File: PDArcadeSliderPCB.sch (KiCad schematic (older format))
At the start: 8 parts, among them J1 Conn_01x06_Male, J2 Conn_01x06_Male, U1 testsensorg, U2 testsensorg, U3 testsensorg, U4 testsensorg, U5 testsensorg, U6 testsensorg

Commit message: some changes for beauty
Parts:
- removed U1, U2, U3, U4, U5, U6: testsensorg, testlibrary:sensorg, symbol testsensorlib:testsensorg
- added U1, U2, U3, U4, U5, U6: testsensorg, symbol test:testsensorg
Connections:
- wire segments 23 -> 21
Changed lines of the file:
@@
 EESchema Schematic File Version 4
-EELAYER 26 0
+EELAYER 30 0
 EELAYER END
 $Descr A4 11693 8268
@@
 	1    0    0    -1
 $EndComp
-$Comp
-L testsensorlib:testsensorg U1
-U 1 1 5C3C1C0C
-P 8100 2600
-F 0 "U1" H 8678 2046 50  0000 L CNN
-F 1 "testsensorg" H 8678 1955 50  0000 L CNN
-F 2 "testlibrary:sensorg" H 8100 2600 50  0001 C CNN
-F 3 "" H 8100 2600 50  0001 C CNN
-	1    8100 2600
-	1    0    0    -1
-$EndComp
-Wire Wire Line
-	8200 3200 7800 3200
 Wire Wire Line
 	7800 3200 7800 3400
 Wire Wire Line
 	7800 3400 7500 3400
-$Comp
-L testsensorlib:testsensorg U4
-U 1 1 5C3C1D40
-P 8500 2800
-F 0 "U4" H 9078 2246 50  0000 L CNN
-F 1 "testsensorg" H 9078 2155 50  0000 L CNN
-F 2 "testlibrary:sensorg" H 8500 2800 50  0001 C CNN
-F 3 "" H 8500 2800 50  0001 C CNN
-	1    8500 2800
-	1    0    0    -1
-$EndComp
-$Comp
-L testsensorlib:testsensorg U2
-U 1 1 5C3C1DA6
-P 8100 3000
-F 0 "U2" H 8678 2446 50  0000 L CNN
-F 1 "testsensorg" H 8678 2355 50  0000 L CNN
-F 2 "testlibrary:sensorg" H 8100 3000 50  0001 C CNN
-F 3 "" H 8100 3000 50  0001 C CNN
-	1    8100 3000
-	1    0    0    -1
-$EndComp
-$Comp
-L testsensorlib:testsensorg U5
-U 1 1 5C3C1E08
-P 8500 3200
-F 0 "U5" H 9078 2646 50  0000 L CNN
-F 1 "testsensorg" H 9078 2555 50  0000 L CNN
-F 2 "testlibrary:sensorg" H 8500 3200 50  0001 C CNN
-F 3 "" H 8500 3200 50  0001 C CNN
-	1    8500 3200
-	1    0    0    -1
-$EndComp
-$Comp
-L testsensorlib:testsensorg U3
-U 1 1 5C3C1E58
-P 8100 3400
-F 0 "U3" H 8678 2846 50  0000 L CNN
-F 1 "testsensorg" H 8678 2755 50  0000 L CNN
-F 2 "testlibrary:sensorg" H 8100 3400 50  0001 C CNN
-F 3 "" H 8100 3400 50  0001 C CNN
-	1    8100 3400
-	1    0    0    -1
-$EndComp
-$Comp
-L testsensorlib:testsensorg U6
-U 1 1 5C3C1E94
-P 8500 3600
-F 0 "U6" H 9078 3046 50  0000 L CNN
-F 1 "testsensorg" H 9078 2955 50  0000 L CNN
-F 2 "testlibrary:sensorg" H 8500 3600 50  0001 C CNN
-F 3 "" H 8500 3600 50  0001 C CNN
-	1    8500 3600
-	1    0    0    -1
-$EndComp
-Wire Wire Line
-	8600 3400 7850 3400
 Wire Wire Line
 	7850 3400 7850 3500
 Wire Wire Line
 	7850 3500 7500 3500
-Wire Wire Line
-	7500 3600 8200 3600
-Wire Wire Line
-	8250 3700 8250 3800
-Wire Wire Line
-	8250 3800 8600 3800
-Wire Wire Line
-	7500 3700 8250 3700
-Wire Wire Line
-	8200 4000 8200 3800
-Wire Wire Line
-	8200 3800 7500 3800
-Wire Wire Line
-	8600 4200 8100 4200
-Wire Wire Line
-	8100 4200 8100 3900
-Wire Wire Line
-	8100 3900 7500 3900
 $Comp
 L Connector:Conn_01x06_Male J2
@@
 $EndComp
 Wire Wire Line
-	9250 2850 9250 1450
-Wire Wire Line
-	9250 1450 10350 1450
-Wire Wire Line
 	7500 3400 6950 3400
 Connection ~ 7500 3400
@@
 Wire Wire Line
 	6950 3700 7500 3700
+Wire Wire Line
+	7500 3800 6950 3800
+Wire Wire Line
+	6950 3900 7500 3900
+$Comp
+L test:testsensorg U1
+U 1 1 5DDFA193
+P 8000 2600
+F 0 "U1" H 8578 2046 50  0000 L CNN
+F 1 "testsensorg" H 8578 1955 50  0000 L CNN
+F 2 "" H 8000 2600 50  0001 C CNN
+F 3 "" H 8000 2600 50  0001 C CNN
+	1    8000 2600
+	1    0    0    -1
+$EndComp
+$Comp
+L test:testsensorg U2
+U 1 1 5DDFB269
+P 8000 2800
+F 0 "U2" H 8578 2246 50  0000 L CNN
+F 1 "testsensorg" H 8578 2155 50  0000 L CNN
+F 2 "" H 8000 2800 50  0001 C CNN
+F 3 "" H 8000 2800 50  0001 C CNN
+	1    8000 2800
+	1    0    0    -1
+$EndComp
+$Comp
+L test:testsensorg U3
+U 1 1 5DDFE35C
+P 8000 3000
+F 0 "U3" H 8578 2446 50  0000 L CNN
+F 1 "testsensorg" H 8578 2355 50  0000 L CNN
+F 2 "" H 8000 3000 50  0001 C CNN
+F 3 "" H 8000 3000 50  0001 C CNN
+	1    8000 3000
+	1    0    0    -1
+$EndComp
+Wire Wire Line
+	7500 3600 8100 3600
+$Comp
+L test:testsensorg U4
+U 1 1 5DE011FA
+P 8000 3200
+F 0 "U4" H 8578 2646 50  0000 L CNN
+F 1 "testsensorg" H 8578 2555 50  0000 L CNN
+F 2 "" H 8000 3200 50  0001 C CNN
+F 3 "" H 8000 3200 50  0001 C CNN
+	1    8000 3200
+	1    0    0    -1
+$EndComp
+$Comp
+L test:testsensorg U5
+U 1 1 5DE01935
+P 8000 3400
+F 0 "U5" H 8578 2846 50  0000 L CNN
+F 1 "testsensorg" H 8578 2755 50  0000 L CNN
+F 2 "" H 8000 3400 50  0001 C CNN
+F 3 "" H 8000 3400 50  0001 C CNN
+	1    8000 3400
+	1    0    0    -1
+$EndComp
+$Comp
+L test:testsensorg U6
+U 1 1 5DE01F95
+P 8000 3600
+F 0 "U6" H 8578 3046 50  0000 L CNN
+F 1 "testsensorg" H 8578 2955 50  0000 L CNN
+F 2 "" H 8000 3600 50  0001 C CNN
+F 3 "" H 8000 3600 50  0001 C CNN
+	1    8000 3600
+	1    0    0    -1
+$EndComp
+Wire Wire Line
+	7850 3400 8100 3400
+Wire Wire Line
+	7800 3200 8100 3200
+Wire Wire Line
+	7500 3700 8100 3700
+Wire Wire Line
+	8100 3700 8100 3800
 Connection ~ 7500 3700
 Wire Wire Line
-	7500 3800 6950 3800
+	7500 3800 8050 3800
+Wire Wire Line
+	8050 3800 8050 4000
+Wire Wire Line
+	8050 4000 8100 4000
 Connection ~ 7500 3800
 Wire Wire Line
-	6950 3900 7500 3900
+	7500 3900 8000 3900
+Wire Wire Line
+	8000 3900 8000 4200
+Wire Wire Line
+	8000 4200 8100 4200
 Connection ~ 7500 3900
 $EndSCHEMATC

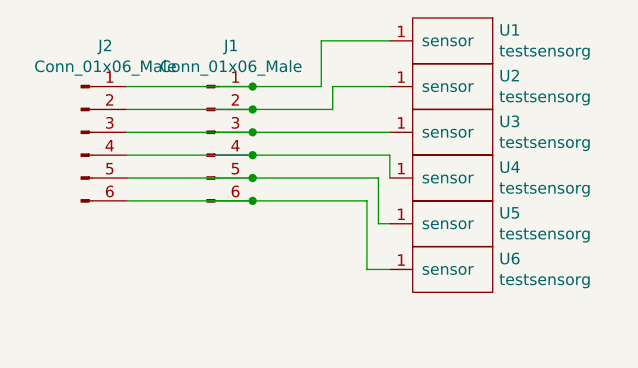
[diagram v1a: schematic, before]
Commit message: Added ground hatching to PCB
Added ground hatching to PCB to decrease parasitic capacitance
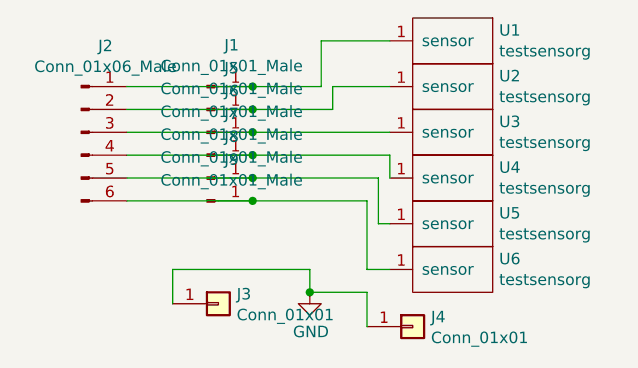
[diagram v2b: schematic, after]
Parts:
- removed J1: Conn_01x06_Male, Connector_PinHeader_1.27mm:PinHeader_1x06_P1.27mm_Vertical, symbol Connector:Conn_01x06_Male
- added J1, J5, J6, J7, J8, J9: Conn_01x01_Male, Connector_PinHeader_1.27mm:PinHeader_1x01_P1.27mm_Vertical, symbol Connector:Conn_01x01_Male
- added J3, J4: Conn_01x01, Connector_PinSocket_2.54mm:PinSocket_1x01_P2.54mm_Horizontal, symbol Connector_Generic:Conn_01x01
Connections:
- net at J2.1 (Pin_1), U1.1 (sensor): now also J1.1 (Pin_1)
- net at J2.2 (Pin_2), U2.1 (sensor): now also J5.1 (Pin_1)
- net at J2.3 (Pin_3), U3.1 (sensor): now also J6.1 (Pin_1)
- net at J2.4 (Pin_4), U4.1 (sensor): now also J7.1 (Pin_1)
- net at J2.5 (Pin_5), U5.1 (sensor): now also J8.1 (Pin_1)
- net at J2.6 (Pin_6), U6.1 (sensor): now also J9.1 (Pin_1)
- new net GND: J3.1 (Pin_1), J4.1 (Pin_1)
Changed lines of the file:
@@
-EESchema Schematic File Version 4
+EESchema Schematic File Version 5
 EELAYER 30 0
 EELAYER END
@@
 Comment3 ""
 Comment4 ""
+Comment5 ""
+Comment6 ""
+Comment7 ""
+Comment8 ""
+Comment9 ""
 $EndDescr
-$Comp
-L Connector:Conn_01x06_Male J1
-U 1 1 5C3BAF9E
-P 7300 3600
-F 0 "J1" H 7406 3978 50  0000 C CNN
-F 1 "Conn_01x06_Male" H 7406 3887 50  0000 C CNN
-F 2 "Connector_PinHeader_1.27mm:PinHeader_1x06_P1.27mm_Vertical" H 7300 3600 50  0001 C CNN
-F 3 "~" H 7300 3600 50  0001 C CNN
-	1    7300 3600
-	1    0    0    -1
-$EndComp
 Wire Wire Line
 	7800 3200 7800 3400
 Wire Wire Line
-	7800 3400 7500 3400
-Wire Wire Line
 	7850 3400 7850 3500
-Wire Wire Line
-	7850 3500 7500 3500
 $Comp
 L Connector:Conn_01x06_Male J2
@@
 	1    0    0    -1
 $EndComp
-Wire Wire Line
-	7500 3400 6950 3400
-Connection ~ 7500 3400
-Wire Wire Line
-	6950 3500 7500 3500
-Connection ~ 7500 3500
-Wire Wire Line
-	7500 3600 6950 3600
-Connection ~ 7500 3600
-Wire Wire Line
-	6950 3700 7500 3700
-Wire Wire Line
-	7500 3800 6950 3800
-Wire Wire Line
-	6950 3900 7500 3900
 $Comp
 L test:testsensorg U1
@@
 	1    0    0    -1
 $EndComp
-Wire Wire Line
-	7500 3600 8100 3600
 $Comp
 L test:testsensorg U4
@@
 	7800 3200 8100 3200
 Wire Wire Line
+	8100 3700 8100 3800
+Wire Wire Line
+	8050 3800 8050 4000
+Wire Wire Line
+	8050 4000 8100 4000
+Wire Wire Line
+	8000 3900 8000 4200
+Wire Wire Line
+	8000 4200 8100 4200
+$Comp
+L power:GND #PWR0101
+U 1 1 5DEF6165
+P 7750 4300
+F 0 "#PWR0101" H 7750 4050 50  0001 C CNN
+F 1 "GND" H 7755 4127 50  0000 C CNN
+F 2 "" H 7750 4300 50  0001 C CNN
+F 3 "" H 7750 4300 50  0001 C CNN
+	1    7750 4300
+	1    0    0    -1
+$EndComp
+$Comp
+L Connector_Generic:Conn_01x01 J3
+U 1 1 5DEF9922
+P 7350 4350
+F 0 "J3" H 7430 4392 50  0000 L CNN
+F 1 "Conn_01x01" H 7430 4301 50  0000 L CNN
+F 2 "Connector_PinSocket_2.54mm:PinSocket_1x01_P2.54mm_Horizontal" H 7350 4350 50  0001 C CNN
+F 3 "~" H 7350 4350 50  0001 C CNN
+	1    7350 4350
+	1    0    0    -1
+$EndComp
+$Comp
+L Connector_Generic:Conn_01x01 J4
+U 1 1 5DEFB162
+P 8200 4450
+F 0 "J4" H 8280 4492 50  0000 L CNN
+F 1 "Conn_01x01" H 8280 4401 50  0000 L CNN
+F 2 "Connector_PinSocket_2.54mm:PinSocket_1x01_P2.54mm_Horizontal" H 8200 4450 50  0001 C CNN
+F 3 "~" H 8200 4450 50  0001 C CNN
+	1    8200 4450
+	1    0    0    -1
+$EndComp
+Wire Wire Line
+	8000 4450 8000 4300
+Wire Wire Line
+	8000 4300 7750 4300
+Connection ~ 7750 4300
+Wire Wire Line
+	7150 4350 7150 4200
+Wire Wire Line
+	7150 4200 7750 4200
+Wire Wire Line
+	7750 4200 7750 4300
+Wire Wire Line
+	6950 3400 7500 3400
+Wire Wire Line
+	7500 3400 7800 3400
+Connection ~ 7500 3400
+$Comp
+L Connector:Conn_01x01_Male J1
+U 1 1 5DEF97FC
+P 7300 3400
+F 0 "J1" H 7408 3581 50  0000 C CNN
+F 1 "Conn_01x01_Male" H 7408 3490 50  0000 C CNN
+F 2 "Connector_PinHeader_1.27mm:PinHeader_1x01_P1.27mm_Vertical" H 7300 3400 50  0001 C CNN
+F 3 "~" H 7300 3400 50  0001 C CNN
+	1    7300 3400
+	1    0    0    -1
+$EndComp
+$Comp
+L Connector:Conn_01x01_Male J5
+U 1 1 5DF163F7
+P 7300 3500
+F 0 "J5" H 7408 3681 50  0000 C CNN
+F 1 "Conn_01x01_Male" H 7408 3590 50  0000 C CNN
+F 2 "Connector_PinHeader_1.27mm:PinHeader_1x01_P1.27mm_Vertical" H 7300 3500 50  0001 C CNN
+F 3 "~" H 7300 3500 50  0001 C CNN
+	1    7300 3500
+	1    0    0    -1
+$EndComp
+Wire Wire Line
+	7850 3500 7500 3500
+Wire Wire Line
+	7500 3500 6950 3500
+Connection ~ 7500 3500
+$Comp
+L Connector:Conn_01x01_Male J6
+U 1 1 5DF16DC5
+P 7300 3600
+F 0 "J6" H 7408 3781 50  0000 C CNN
+F 1 "Conn_01x01_Male" H 7408 3690 50  0000 C CNN
+F 2 "Connector_PinHeader_1.27mm:PinHeader_1x01_P1.27mm_Vertical" H 7300 3600 50  0001 C CNN
+F 3 "~" H 7300 3600 50  0001 C CNN
+	1    7300 3600
+	1    0    0    -1
+$EndComp
+Wire Wire Line
+	8100 3600 7500 3600
+Wire Wire Line
+	7500 3600 6950 3600
+Connection ~ 7500 3600
+$Comp
+L Connector:Conn_01x01_Male J7
+U 1 1 5DF176CB
+P 7300 3700
+F 0 "J7" H 7408 3881 50  0000 C CNN
+F 1 "Conn_01x01_Male" H 7408 3790 50  0000 C CNN
+F 2 "Connector_PinHeader_1.27mm:PinHeader_1x01_P1.27mm_Vertical" H 7300 3700 50  0001 C CNN
+F 3 "~" H 7300 3700 50  0001 C CNN
+	1    7300 3700
+	1    0    0    -1
+$EndComp
+$Comp
+L Connector:Conn_01x01_Male J8
+U 1 1 5DF18014
+P 7300 3800
+F 0 "J8" H 7408 3981 50  0000 C CNN
+F 1 "Conn_01x01_Male" H 7408 3890 50  0000 C CNN
+F 2 "Connector_PinHeader_1.27mm:PinHeader_1x01_P1.27mm_Vertical" H 7300 3800 50  0001 C CNN
+F 3 "~" H 7300 3800 50  0001 C CNN
+	1    7300 3800
+	1    0    0    -1
+$EndComp
+$Comp
+L Connector:Conn_01x01_Male J9
+U 1 1 5DF18CAB
+P 7300 3900
+F 0 "J9" H 7408 4081 50  0000 C CNN
+F 1 "Conn_01x01_Male" H 7408 3990 50  0000 C CNN
+F 2 "Connector_PinHeader_1.27mm:PinHeader_1x01_P1.27mm_Vertical" H 7300 3900 50  0001 C CNN
+F 3 "~" H 7300 3900 50  0001 C CNN
+	1    7300 3900
+	1    0    0    -1
+$EndComp
+Wire Wire Line
+	6950 3900 7500 3900
+Connection ~ 7500 3900
+Wire Wire Line
+	7500 3900 8000 3900
+Wire Wire Line
+	6950 3800 7500 3800
+Connection ~ 7500 3800
+Wire Wire Line
+	7500 3800 8050 3800
+Wire Wire Line
+	6950 3700 7500 3700
+Connection ~ 7500 3700
+Wire Wire Line
 	7500 3700 8100 3700
-Wire Wire Line
-	8100 3700 8100 3800
-Connection ~ 7500 3700
-Wire Wire Line
-	7500 3800 8050 3800
-Wire Wire Line
-	8050 3800 8050 4000
-Wire Wire Line
-	8050 4000 8100 4000
-Connection ~ 7500 3800
-Wire Wire Line
-	7500 3900 8000 3900
-Wire Wire Line
-	8000 3900 8000 4200
-Wire Wire Line
-	8000 4200 8100 4200
-Connection ~ 7500 3900
 $EndSCHEMATC

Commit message: Trying to find better hatching settings
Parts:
- J2: footprint testlibrary:testtt -> test:testtt
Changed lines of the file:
@@
 F 0 "J2" H 6856 3978 50  0000 C CNN
 F 1 "Conn_01x06_Male" H 6856 3887 50  0000 C CNN
-F 2 "testlibrary:testtt" H 6750 3600 50  0001 C CNN
+F 2 "test:testtt" H 6750 3600 50  0001 C CNN
 F 3 "~" H 6750 3600 50  0001 C CNN
 	1    6750 3600

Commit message: Ground hatching from old manual
Ground hatching from old manual
https://forum.kicad.info/t/copper-pour-with-hatched-fill-instead-of-solid-fill/860/8
because for now KiCad cannot make hatching like this
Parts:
- added J10: topgroundhatching, PDArcadeSliderPCB:TopHatching, symbol PDArcadeSliderPCBsensorlib:topgroundhatching
- added J?: topgroundhatching, PDArcadeSliderPCB:bottomhatching, symbol PDArcadeSliderPCBsensorlib:topgroundhatching
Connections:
- wire segments 26 -> 32
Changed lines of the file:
@@
-	1    0    0    -1
-$EndComp
-$Comp
-L Connector_Generic:Conn_01x01 J4
-U 1 1 5DEFB162
-P 8200 4450
-F 0 "J4" H 8280 4492 50  0000 L CNN
-F 1 "Conn_01x01" H 8280 4401 50  0000 L CNN
-F 2 "Connector_PinSocket_2.54mm:PinSocket_1x01_P2.54mm_Horizontal" H 8200 4450 50  0001 C CNN
-F 3 "~" H 8200 4450 50  0001 C CNN
-	1    8200 4450
 	1    0    0    -1
 $EndComp
@@
 Wire Wire Line
 	7500 3700 8100 3700
+Wire Wire Line
+	7650 4300 7750 4300
+$Comp
+L Connector_Generic:Conn_01x01 J4
+U 1 1 5DEFB162
+P 8200 4450
+F 0 "J4" H 8280 4492 50  0000 L CNN
+F 1 "Conn_01x01" H 8280 4401 50  0000 L CNN
+F 2 "Connector_PinSocket_2.54mm:PinSocket_1x01_P2.54mm_Horizontal" H 8200 4450 50  0001 C CNN
+F 3 "~" H 8200 4450 50  0001 C CNN
+	1    8200 4450
+	1    0    0    -1
+$EndComp
+$Comp
+L PDArcadeSliderPCBsensorlib:topgroundhatching J10
+U 1 1 5DF7238E
+P 7850 4750
+F 0 "J10" H 7930 4792 50  0000 L CNN
+F 1 "topgroundhatching" H 7930 4701 50  0000 L CNN
+F 2 "PDArcadeSliderPCB:TopHatching" H 7850 4750 50  0001 C CNN
+F 3 "~" H 7850 4750 50  0001 C CNN
+	1    7850 4750
+	1    0    0    -1
+$EndComp
+Wire Wire Line
+	7650 4300 7650 4750
+$Comp
+L PDArcadeSliderPCBsensorlib:topgroundhatching J?
+U 1 1 5DF747A8
+P 8900 4700
+F 0 "J?" H 8980 4742 50  0000 L CNN
+F 1 "topgroundhatching" H 8980 4651 50  0000 L CNN
+F 2 "PDArcadeSliderPCB:bottomhatching" H 8900 4700 50  0001 C CNN
+F 3 "~" H 8900 4700 50  0001 C CNN
+	1    8900 4700
+	1    0    0    -1
+$EndComp
+Wire Wire Line
+	8700 4700 8100 4700
+Wire Wire Line
+	8100 4700 8100 4900
+Wire Wire Line
+	8100 4900 7650 4900
+Wire Wire Line
+	7650 4900 7650 4750
+Connection ~ 7650 4750
 $EndSCHEMATC

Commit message: Version with ground hatching failed. Changes and fixes
without ground hatching
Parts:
- gave numbers to parts that had none: 1

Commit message: little bigger pads, deleted trash
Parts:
- removed J10: topgroundhatching, PDArcadeSliderPCB:TopHatching, symbol PDArcadeSliderPCBsensorlib:topgroundhatching
- removed J11: topgroundhatching, PDArcadeSliderPCB:bottomhatching, symbol PDArcadeSliderPCBsensorlib:topgroundhatching
- removed J3, J4: Conn_01x01, Connector_PinSocket_2.54mm:PinSocket_1x01_P2.54mm_Horizontal, symbol Connector_Generic:Conn_01x01
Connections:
- net labels removed: GND
- wire segments 32 -> 21
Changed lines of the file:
@@
 Connection ~ 7500 3800
 Connection ~ 7500 3900
-Connection ~ 7650 4750
-Connection ~ 7750 4300
 Wire Wire Line
 	6950 3400 7500 3400
@@
 Wire Wire Line
 	6950 3900 7500 3900
-Wire Wire Line
-	7150 4200 7750 4200
-Wire Wire Line
-	7150 4350 7150 4200
 Wire Wire Line
 	7500 3400 7800 3400
@@
 Wire Wire Line
 	7500 3900 8000 3900
-Wire Wire Line
-	7650 4300 7650 4750
-Wire Wire Line
-	7650 4300 7750 4300
-Wire Wire Line
-	7650 4900 7650 4750
-Wire Wire Line
-	7750 4200 7750 4300
 Wire Wire Line
 	7800 3200 7800 3400
@@
 	8000 4200 8100 4200
 Wire Wire Line
-	8000 4300 7750 4300
-Wire Wire Line
-	8000 4450 8000 4300
-Wire Wire Line
 	8050 3800 8050 4000
 Wire Wire Line
@@
 Wire Wire Line
 	8100 3700 8100 3800
-Wire Wire Line
-	8100 4700 8100 4900
-Wire Wire Line
-	8100 4900 7650 4900
-Wire Wire Line
-	8700 4700 8100 4700
-$Comp
-L power:GND #PWR0101
-U 1 1 5DEF6165
-P 7750 4300
-F 0 "#PWR0101" H 7750 4050 50  0001 C CNN
-F 1 "GND" H 7755 4127 50  0000 C CNN
-F 2 "" H 7750 4300 50  0001 C CNN
-F 3 "" H 7750 4300 50  0001 C CNN
-	1    7750 4300
-	1    0    0    -1
-$EndComp
 $Comp
 L Connector:Conn_01x01_Male J1
@@
 	1    0    0    -1
 $EndComp
-$Comp
-L Connector_Generic:Conn_01x01 J3
-U 1 1 5DEF9922
-P 7350 4350
-F 0 "J3" H 7430 4392 50  0000 L CNN
-F 1 "Conn_01x01" H 7430 4301 50  0000 L CNN
-F 2 "Connector_PinSocket_2.54mm:PinSocket_1x01_P2.54mm_Horizontal" H 7350 4350 50  0001 C CNN
-F 3 "~" H 7350 4350 50  0001 C CNN
-	1    7350 4350
-	1    0    0    -1
-$EndComp
-$Comp
-L PDArcadeSliderPCBsensorlib:topgroundhatching J10
-U 1 1 5DF7238E
-P 7850 4750
-F 0 "J10" H 7930 4792 50  0000 L CNN
-F 1 "topgroundhatching" H 7930 4701 50  0000 L CNN
-F 2 "PDArcadeSliderPCB:TopHatching" H 7850 4750 50  0001 C CNN
-F 3 "~" H 7850 4750 50  0001 C CNN
-	1    7850 4750
-	1    0    0    -1
-$EndComp
-$Comp
-L Connector_Generic:Conn_01x01 J4
-U 1 1 5DEFB162
-P 8200 4450
-F 0 "J4" H 8280 4492 50  0000 L CNN
-F 1 "Conn_01x01" H 8280 4401 50  0000 L CNN
-F 2 "Connector_PinSocket_2.54mm:PinSocket_1x01_P2.54mm_Horizontal" H 8200 4450 50  0001 C CNN
-F 3 "~" H 8200 4450 50  0001 C CNN
-	1    8200 4450
-	1    0    0    -1
-$EndComp
-$Comp
-L PDArcadeSliderPCBsensorlib:topgroundhatching J11
-U 1 1 5DF747A8
-P 8900 4700
-F 0 "J11" H 8980 4742 50  0000 L CNN
-F 1 "topgroundhatching" H 8980 4651 50  0000 L CNN
-F 2 "PDArcadeSliderPCB:bottomhatching" H 8900 4700 50  0001 C CNN
-F 3 "~" H 8900 4700 50  0001 C CNN
-	1    8900 4700
-	1    0    0    -1
-$EndComp
